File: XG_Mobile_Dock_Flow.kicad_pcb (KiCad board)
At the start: 4 copper layers, 220 x 65 mm, 57 parts, among them J1 5-1775443-8, J10 SWD, J11 UART, J12 I2C1, J13 39300240, J14 469911008, J17 8730, J2 20455-040E-76, J3 20455-040E-76, J4 3-2362375-4, J5 USB_C_Receptacle, Q16 AO3401A, Q17 2N7002W, SW1 SW_Push, U12 STM32F030C8Tx

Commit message: more pcb changes
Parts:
- added C1: 0.22μF, Capacitor_SMD:C_0201_0603Metric, F.Cu at (93.0, 66.4)
- added C10: 0.22μF, Capacitor_SMD:C_0201_0603Metric, F.Cu at (112.9, 66.6)
- added C11: 0.22μF, Capacitor_SMD:C_0201_0603Metric, F.Cu at (116.0, 66.6)
- added C12: 0.22μF, Capacitor_SMD:C_0201_0603Metric, F.Cu at (116.9, 66.6)
- added C13: 0.22μF, Capacitor_SMD:C_0201_0603Metric, F.Cu at (120.0, 66.6)
- added C14: 0.22μF, Capacitor_SMD:C_0201_0603Metric, F.Cu at (120.9, 66.6)
- added C15: 0.22μF, Capacitor_SMD:C_0201_0603Metric, F.Cu at (124.0, 66.7)
- added C16: 0.22μF, Capacitor_SMD:C_0201_0603Metric, F.Cu at (124.9, 66.7)
- added C17: 0.1μF, Capacitor_SMD:C_0201_0603Metric, B.Cu at (103.8, 76.6)
- added C18: 0.1μF, Capacitor_SMD:C_0201_0603Metric, B.Cu at (104.8, 76.6)
- added C19: 0.1μF, Capacitor_SMD:C_0201_0603Metric, B.Cu at (105.7, 76.6)
- added C2: 0.22μF, Capacitor_SMD:C_0201_0603Metric, F.Cu at (93.9, 66.4)
- added C20: 0.1μF, Capacitor_SMD:C_0201_0603Metric, B.Cu at (106.6, 76.6)
- added C21: 1μF, Capacitor_SMD:C_0201_0603Metric, F.Cu at (48.8, 0.67)
- added C22: 0.1μF, Capacitor_SMD:C_0201_0603Metric, F.Cu at (55.3, 0.28)
- added C23: 0.1μF, Capacitor_SMD:C_0201_0603Metric, F.Cu at (51.2, -8.08)
- added C24: 0.1μF, Capacitor_SMD:C_0201_0603Metric, F.Cu at (51.2, -6.33)
- added C25: 0.1μF, Capacitor_SMD:C_0201_0603Metric, F.Cu at (51.2, -4.58)
- added C26: 1μF, Capacitor_SMD:C_0201_0603Metric, F.Cu at (51.2, -2.83)
- added C3: 0.22μF, Capacitor_SMD:C_0201_0603Metric, F.Cu at (98.0, 66.5)
- added C4: 0.22μF, Capacitor_SMD:C_0201_0603Metric, F.Cu at (98.9, 66.5)
- added C5: 0.22μF, Capacitor_SMD:C_0201_0603Metric, F.Cu at (102.0, 66.5)
- added C6: 0.22μF, Capacitor_SMD:C_0201_0603Metric, F.Cu at (102.9, 66.5)
- added C7: 0.22μF, Capacitor_SMD:C_0201_0603Metric, F.Cu at (106.0, 66.5)
- added C8: 0.22μF, Capacitor_SMD:C_0201_0603Metric, F.Cu at (106.9, 66.5)
- added C9: 0.22μF, Capacitor_SMD:C_0201_0603Metric, F.Cu at (112.0, 66.6)
- added J16: ~, Connector_JST:JST_PH_S2B-PH-K_1x02_P2.00mm_Horizontal, F.Cu at (59.3, -8.33)
- added R64: 1k, Resistor_SMD:R_0402_1005Metric, F.Cu at (111.0, 78.2)
- added R65: 1k, Resistor_SMD:R_0402_1005Metric, F.Cu at (128.1, 78.8)
- added R66: 59k, Resistor_SMD:R_0402_1005Metric, F.Cu at (128.1, 71.8)
- added R67: 59k, Resistor_SMD:R_0402_1005Metric, F.Cu at (128.1, 70.0)
- added R68: 59k, Resistor_SMD:R_0402_1005Metric, F.Cu at (111.0, 71.8)
- added R69: 59k, Resistor_SMD:R_0402_1005Metric, F.Cu at (111.0, 70.1)
- added R70: 4.7k, Resistor_SMD:R_0402_1005Metric, F.Cu at (111.0, 76.7)
- added R71: 4.7k, Resistor_SMD:R_0402_1005Metric, F.Cu at (111.0, 75.0)
- added R72: 4.7k, Resistor_SMD:R_0402_1005Metric, F.Cu at (99.6, 74.0)
- added R73: 4.7k, Resistor_SMD:R_0402_1005Metric, F.Cu at (116.2, 73.8)
- added R74: 47k, Resistor_SMD:R_0402_1005Metric, F.Cu at (65.7, -9.71)
- added R78: 4.7k, Resistor_SMD:R_0402_1005Metric, F.Cu at (128.1, 77.4)
- added R79: 4.7k, Resistor_SMD:R_0402_1005Metric, F.Cu at (128.0, 75.4)
- added R80: 4.7k, Resistor_SMD:R_0402_1005Metric, F.Cu at (99.6, 72.2)
- added R81: 4.7k, Resistor_SMD:R_0402_1005Metric, F.Cu at (99.6, 75.6)
- added R82: 4.7k, Resistor_SMD:R_0402_1005Metric, F.Cu at (116.2, 75.4)
- added R83: 59k, Resistor_SMD:R_0402_1005Metric, F.Cu at (111.0, 73.7)
- added R87: 59k, Resistor_SMD:R_0402_1005Metric, F.Cu at (128.1, 73.8)
- added R88: 1k, Resistor_SMD:R_0402_1005Metric, F.Cu at (99.6, 77.4)
- added R89: 1k, Resistor_SMD:R_0402_1005Metric, F.Cu at (116.2, 77.2)
- added R90: 4.7k, Resistor_SMD:R_0402_1005Metric, F.Cu at (116.1, 72.2)
- added U1: DS160PR410RNQR, DS160PR410RNQR:WQFN_RNQ40_TEX, F.Cu at (105.2, 74.5)
- added U2: DS160PR410RNQR, DS160PR410RNQR:WQFN_RNQ40_TEX, F.Cu at (121.7, 74.7)
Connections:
- J2 pad 1: /HSO6N -> /HSOL6N
- J2 pad 13: /HSO4N -> /HSOL4N
- J2 pad 14: /HSO4P -> /HSOL4P
- J2 pad 19: /HSO3N -> /HSOL3N
- J2 pad 2: /HSO6P -> /HSOL6P
- J2 pad 20: /HSO3P -> /HSOL3P
- J2 pad 25: /HSO2N -> /HSOL2N
- J2 pad 26: /HSO2P -> /HSOL2P
- J2 pad 31: /HSO1N -> /HSOL1N
- J2 pad 32: /HSO1P -> /HSOL1P
- J2 pad 37: /HSO0N -> /HSOL0N
- J2 pad 38: /HSO0P -> /HSOL0P
- J2 pad 7: /HSO5N -> /HSOL5N
- J2 pad 8: /HSO5P -> /HSOL5P
- J3 pad 36: /HSO7N -> /HSOL7N
- J3 pad 37: /HSO7P -> /HSOL7P
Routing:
- net /HSO0P: track 26.3 -> 2.64 mm
- net /HSO0N: track 26.3 -> 2.64 mm
- net /HSO7N: track 26.1 -> 2.89 mm
- net /HSO7P: track 26.1 -> 2.89 mm
- net /HSO1P: track 25.4 -> 2.74 mm
- net /HSO1N: track 25.4 -> 2.74 mm
- net /HSO2N: track 25.0 -> 2.75 mm
- net /HSO2P: track 25.0 -> 2.75 mm
- net /HSO3P: track 24.6 -> 2.74 mm
- net /HSO3N: track 24.9 -> 3.00 mm
- net /HSO6P: track 24.5 -> 2.81 mm
- net /HSO6N: track 24.5 -> 2.81 mm
- net /HSO5P: track 24.0 -> 2.78 mm
- net /HSO5N: track 24.0 -> 2.78 mm
- net /HSO4P: track 23.6 -> 2.84 mm
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
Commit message: almost finished everything
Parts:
- added C27: 0.1μF, Capacitor_SMD:C_0201_0603Metric, B.Cu at (106.7, 72.5)
- added C28: 0.1μF, Capacitor_SMD:C_0201_0603Metric, B.Cu at (103.8, 72.5)
- added C29: 0.1μF, Capacitor_SMD:C_0201_0603Metric, B.Cu at (120.3, 72.7)
- added C30: 0.1μF, Capacitor_SMD:C_0201_0603Metric, B.Cu at (123.1, 72.7)
- C21, C22, C23, C24, C25, C26: moved to B.Cu
- moved C23 111.2 mm to (123.1, 76.8), turned to -90 degrees
- moved C24 109.3 mm to (122.2, 76.8), turned to -90 degrees
- moved C26 108.4 mm to (122.2, 79.1), turned to 180 degrees
- moved C25 107.4 mm to (121.2, 76.8), turned to -90 degrees
- moved C22 100.4 mm to (120.2, 76.8), turned to -90 degrees
- moved C21 96.3 mm to (105.8, 78.3), turned to 180 degrees
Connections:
- U1 pad 11: unconnected-(U1-VREG-Pad11) -> Net-(U1-VREG)
- U1 pad 18: unconnected-(U1-VREF-Pad18) -> Net-(U1-VREF)
- U2 pad 11: unconnected-(U2-VREG-Pad11) -> Net-(U2-VREG)
- U2 pad 18: unconnected-(U2-VREF-Pad18) -> Net-(U2-VREF)
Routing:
- net +3V3: track 159.9 -> 264.8 mm, vias 33 -> 42
- net Net-(U2-VREF): track 0.00 -> 1.49 mm, vias 0 -> 1
- net Net-(U1-VREG): track 0.00 -> 1.49 mm, vias 0 -> 1
- net Net-(U1-VREF): track 0.00 -> 1.46 mm, vias 0 -> 1
- net Net-(U2-VREG): track 0.00 -> 1.44 mm, vias 0 -> 1
- net GND: vias 46 -> 50

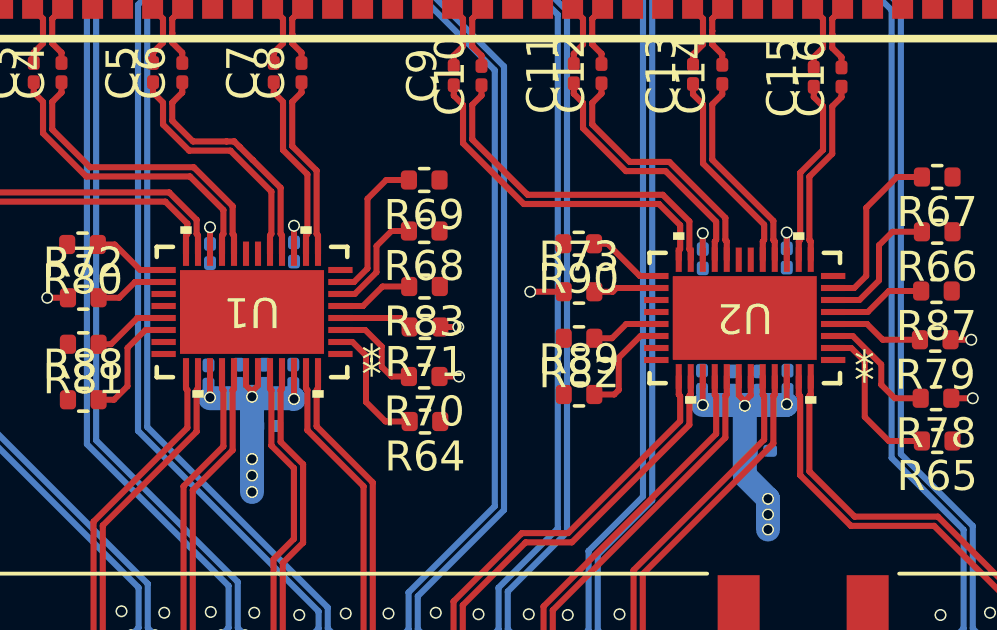
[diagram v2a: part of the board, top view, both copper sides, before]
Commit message: fixed wrong 3.3v path
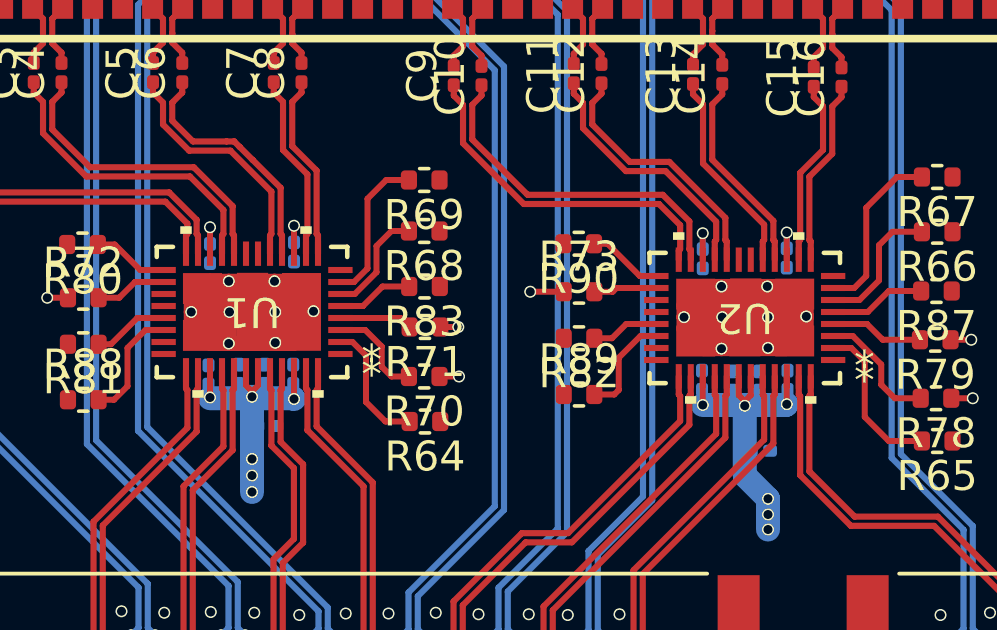
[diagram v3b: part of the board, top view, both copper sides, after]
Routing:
- net GND: track 6.51 -> 61.1 mm, vias 50 -> 66
- net +3V3: track 264.8 -> 217.8 mm

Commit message: routed 3v
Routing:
- net +3V3: track 217.8 -> 228.0 mm
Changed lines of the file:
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@@
+	)
+	(segment
+		(start 129.225 75.425)
+		(end 129.225 77.325)
+		(width 0.8)
+		(layer "In1.Cu")
+		(net 2)
 	)
 	(segment
@@
 		(end 84.917496 72.758603)
 		(width 1.5)
+		(layer "In1.Cu")
+		(net 2)
+	)
+	(segment
+		(start 129.225 77.325)
+		(end 129.275 77.375)
+		(width 0.8)
 		(layer "In1.Cu")
 		(net 2)
@@
 		(layer "In1.Cu")
 		(net 2)
+	)
+	(segment
+		(start 125.925 80.725)
+		(end 122.45 80.725)
+		(width 0.8)
+		(layer "In1.Cu")
+		(net 2)
+	)
+	(segment
+		(start 129.275 77.375)
+		(end 125.925 80.725)
+		(width 0.8)
+		(layer "In1.Cu")
+		(net 2)

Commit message: added thicker 3.3 track in middle layer
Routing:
- net +3V3: track 228.0 -> 237.6 mm
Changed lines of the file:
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@@
+	)
+	(segment
+		(start 143.6 92.725)
+		(end 147.825 88.5)
+		(width 2.045295)
+		(layer "In1.Cu")
+		(net 2)
 	)
 	(segment
@@
 		(end 114.525 73.825)
 		(width 0.8)
-		(layer "In1.Cu")
-		(net 2)
-	)
-	(segment
-		(start 154.33666 76.529018)
-		(end 152.332839 78.532839)
-		(width 1.5)
 		(layer "In1.Cu")
 		(net 2)
@@
 	)
 	(segment
-		(start 122.45 92.154)
-		(end 104.312893 92.154)
-		(width 1.5)
-		(layer "In1.Cu")
-		(net 2)
-	)
-	(segment
 		(start 112.15 76.65)
 		(end 107.925 80.875)
 		(width 0.8)
-		(layer "In1.Cu")
-		(net 2)
-	)
-	(segment
-		(start 147.621496 88.029018)
-		(end 143.496514 92.154)
-		(width 1.5)
 		(layer "In1.Cu")
 		(net 2)
@@
 	)
 	(segment
-		(start 84.917496 72.758603)
-		(end 84.917496 63.377496)
-		(width 1.5)
+		(start 147.825 83.040678)
+		(end 154.33666 76.529018)
+		(width 2.045295)
 		(layer "In1.Cu")
 		(net 2)
 	)
 	(segment
-		(start 97.029446 84.870554)
-		(end 91.079446 78.920554)
-		(width 1.5)
+		(start 104.883893 92.725)
+		(end 143.6 92.725)
+		(width 2.045295)
 		(layer "In1.Cu")
 		(net 2)
@@
 	)
 	(segment
+		(start 154.33666 76.529018)
+		(end 169.83666 76.529018)
+		(width 2.045295)
+		(layer "In1.Cu")
+		(net 2)
+	)
+	(segment
 		(start 98.425 74.025)
 		(end 95.975 74.025)
@@
 	)
 	(segment
-		(start 152.332839 78.532839)
-		(end 147.621496 83.244182)
-		(width 1.5)
+		(start 105.25 80.85)
+		(end 105.275 80.875)
+		(width 1)
 		(layer "In1.Cu")
 		(net 2)
 	)
 	(segment
-		(start 105.25 80.85)
-		(end 105.275 80.875)
-		(width 1)
+		(start 147.825 88.5)
+		(end 147.825 83.040678)
+		(width 2.045295)
+		(layer "In1.Cu")
+		(net 2)
+	)
+	(segment
+		(start 84.917496 72.758603)
+		(end 104.312893 92.154)
+		(width 2.045295)
 		(layer "In1.Cu")
 		(net 2)
@@
 		(end 105.275 80.875)
 		(width 0.8)
-		(layer "In1.Cu")
-		(net 2)
-	)
-	(segment
-		(start 143.496514 92.154)
-		(end 122.45 92.154)
-		(width 1.5)
 		(layer "In1.Cu")
 		(net 2)
@@
 	)
 	(segment
-		(start 147.621496 83.244182)
-		(end 147.621496 88.029018)
-		(width 1.5)
+		(start 113.35 75)
+		(end 114.525 73.825)
+		(width 0.5)
 		(layer "In1.Cu")
 		(net 2)
 	)
 	(segment
-		(start 169.83666 76.529018)
-		(end 154.33666 76.529018)
-		(width 1.5)
+		(start 84.917496 63.377496)
+		(end 84.917496 72.758603)
+		(width 2.045295)
 		(layer "In1.Cu")
 		(net 2)
 	)
 	(segment
-		(start 113.35 75)
-		(end 114.525 73.825)
-		(width 0.5)
+		(start 104.312893 92.154)
+		(end 104.883893 92.725)
+		(width 2.045295)
 		(layer "In1.Cu")
 		(net 2)
@@
 		(layer "In1.Cu")
 		(net 2)
-	)
-	(segment
-		(start 104.312893 92.154)
-		(end 97.029446 84.870554)
-		(width 1.5)
-		(layer "In1.Cu")
-		(net 2)
